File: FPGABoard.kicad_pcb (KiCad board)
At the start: 2 copper layers, 100 x 80 mm, 76 parts, among them P1 JTAG_FPGA, P3 USB_B, P4 CONN_02X07, P5 JTAG, P6 CONN_02X07, P7 CONN_02X07, P8 CONN_02X07, Q1 Q_NMOS_DSG, SW1 SW_PUSH, SW2 SW_PUSH, U1 XC3S50A/VQ100, U2 LM317_SOT223, U3 LM317_SOT223, U4 LM317_SOT223, U5 ATMEGA32U4RC-A, U6 M25P20, Y1 12MHz

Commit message: Layouting
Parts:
- removed REF**: EuroBoard_halb_Type-I_100mmX80mm_holes, EuroBoard_Outline:EuroBoard_halb_Type-I_100mmX80mm_holes
- added P2: CONN_02X03, w_pin_strip:pin_strip_3x2, F.Cu at (183.5, 71.8)
- R15, R17, R18: moved to B.Cu
- moved R8 43.8 mm to (109.2, 83.8)
- moved C17 41.3 mm to (120.0, 82.5)
- moved R4 41.3 mm to (113.0, 82.5)
- moved U2 40.6 mm to (114.3, 89.5)
- moved C16 40.6 mm to (119.4, 87.0)
- moved R2 40.6 mm to (139.7, 89.5)
- moved C20 36.7 mm to (147.3, 92.1)
- moved R10 36.7 mm to (157.5, 92.1)
- moved R6 36.3 mm to (156.2, 96.5)
- moved U4 36.3 mm to (152.4, 90.2)
- moved C21 36.3 mm to (149.2, 96.5)
- moved C19 24.2 mm to (116.8, 106.7)
- moved R5 23.8 mm to (110.5, 106.7)
- moved U3 23.3 mm to (114.3, 113.7)
- moved C18 23.3 mm to (119.4, 111.1)
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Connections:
- U1 pad 82: (no net) -> /Connections/BTN2
- U1 pad 97: (no net) -> /Connections/BTN1
- U5 pad 18: (no net) -> /Connections/C_IO2
- U5 pad 19: (no net) -> /Connections/C_IO3
- U5 pad 25: (no net) -> /Connections/C_IO4
- U5 pad 31: (no net) -> /Connections/C_IO1
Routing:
- net VCC: track 48.4 -> 389.7 mm, vias 0 -> 11
- net VCC_AUX: track 43.3 -> 128.4 mm, vias 1 -> 4
- net Net-(P5-Pad1): track 65.1 -> 0.64 mm, vias 1 -> 0
- net /Microcontroller/SCK: track 91.5 -> 28.2 mm, vias 2 -> 0
- net /Spartan3A/Clock_In: track 63.3 -> 0.00 mm, vias 4 -> 0
- net Net-(P5-Pad3): track 62.2 -> 0.00 mm, vias 1 -> 0
- net Net-(P5-Pad5): track 60.2 -> 0.00 mm, vias 1 -> 0
- net /Microcontroller/MISO: track 67.8 -> 8.01 mm, vias 4 -> 0
- net Net-(P5-Pad9): track 59.7 -> 0.00 mm
- net VCC_INT: track 7.17 -> 65.7 mm, vias 0 -> 4
- net /Microcontroller/CS_FPGA: track 58.2 -> 0.07 mm, vias 2 -> 0
- net /Connections/BTN1: track 0.00 -> 56.6 mm, vias 0 -> 2
- net /Microcontroller/RESET: track 55.3 -> 0.00 mm, vias 2 -> 0
- net /Microcontroller/DONE: track 73.9 -> 22.1 mm, vias 2 -> 0
- net /Microcontroller/PROG_B: track 49.4 -> 3.36 mm, vias 2 -> 0
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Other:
- board outline removed
- net class Supply added: clearance 0.1, trace_width 0.5, via_dia 0.6, via_drill 0.4

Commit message: Layout
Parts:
- added C30: 1µF, Capacitors_SMD:C_0805_HandSoldering, B.Cu at (131.1, 102.4)
- added C31: 1µF, Capacitors_SMD:C_0805_HandSoldering, B.Cu at (173.7, 66.5)
- added C32: 1µF, Capacitors_SMD:C_0805_HandSoldering, B.Cu at (145.5, 93.2)
- added C33: 1µF, Capacitors_SMD:C_0805_HandSoldering, B.Cu at (145.3, 96.5)
- added REF**: EuroBoard_halb_Type-I_100mmX80mm_holes, EuroBoard_Outline:EuroBoard_halb_Type-I_100mmX80mm_holes, F.Cu at (88.4, 140.5)
- added U7: XO53, Oscillator__Crystal_SMD:Oscillator_XO53, F.Cu at (156.5, 111.0)
- C1, C2, C7: moved to F.Cu
- C17, C19, C21: footprint Capacitors_Tantalum_SMD:TantalC_SizeA_EIA-3216_HandSoldering -> Capacitors_SMD:C_0805_HandSoldering
- C22: moved to B.Cu
- C23, C24, C25, C26, C27, C29: footprint Capacitors_SMD:C_0603_HandSoldering -> Capacitors_SMD:C_0805_HandSoldering
- P3: footprint Connect:USB_B -> w_conn_pc:conn_usb_B_mini_smd
- Y1: footprint Crystals:Crystal_HC49-SD_SMD -> w_crystal:hc-49_smd
- moved C1 71.3 mm to (156.7, 107.4), turned to 180 degrees
- moved R10 53.6 mm to (109.5, 115.8)
- moved U4 50.4 mm to (114.3, 123.2), turned to 0 degrees
- moved R6 47.6 mm to (113.3, 117.1), turned to 180 degrees
- moved C21 40.3 mm to (113.3, 114.8)
- moved C20 38.9 mm to (119.1, 118.9)
- moved R18 15.1 mm to (100.3, 108.0)
- moved R17 15.0 mm to (100.3, 105.2)
- moved R15 14.9 mm to (100.3, 102.4)
- moved R9 12.5 mm to (109.7, 99.3), turned to 90 degrees
- moved P3 9.90 mm to (139.5, 66.0), turned to 180 degrees
- moved C19 9.11 mm to (113.3, 98.3), turned to 180 degrees
- moved U3 7.11 mm to (114.3, 106.6)
- moved C17 6.85 mm to (113.3, 81.3), turned to 180 degrees
- moved R5 6.71 mm to (113.3, 100.6)
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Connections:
- D5 pad 1: GND -> Net-(D5-Pad1)
- D5 pad 2: Net-(D5-Pad2) -> /Connections/LED2
- D6 pad 1: GND -> Net-(D6-Pad1)
- D6 pad 2: Net-(D6-Pad2) -> /Connections/LED1
- D7 pad 1: GND -> Net-(D7-Pad1)
- D7 pad 2: Net-(D7-Pad2) -> /Connections/LED3
- P2 pad 1: (no net) -> VCC
- P2 pad 2: (no net) -> GND
- R1 pad 1: /Microcontroller/PROG_B -> Net-(R1-Pad1)
- R15 pad 1: Net-(D5-Pad2) -> GND
- R15 pad 2: /Connections/LED2 -> Net-(D6-Pad1)
- R17 pad 1: Net-(D6-Pad2) -> GND
- R17 pad 2: /Connections/LED1 -> Net-(D5-Pad1)
- R18 pad 1: Net-(D7-Pad2) -> GND
- R18 pad 2: /Connections/LED3 -> Net-(D7-Pad1)
- U1 pad 100: /Microcontroller/PROG_B -> Net-(R1-Pad1)
- U1 pad 90: /Spartan3A/Clock_In -> Net-(U1-Pad90)
- U5 pad 28: /Microcontroller/PROG_B -> (no net)
- U5 pad 32: /Spartan3A/Clock_In -> (no net)
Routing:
- net /Microcontroller/DONE: track 22.1 -> 107.0 mm, vias 0 -> 3
- net /Microcontroller/CS_FPGA: track 0.07 -> 63.8 mm, vias 0 -> 4
- net /Microcontroller/INIT_B: track 6.04 -> 69.3 mm, vias 0 -> 4
- net /Microcontroller/CS_FLASH: track 0.47 -> 59.4 mm, vias 0 -> 3
- net /Microcontroller/SCK: track 28.2 -> 85.7 mm, vias 0 -> 4
- net /Microcontroller/MISO: track 8.01 -> 59.3 mm, vias 0 -> 4
- net /Microcontroller/MOSI: track 26.5 -> 75.5 mm, vias 0 -> 4
- net /Microcontroller/CS_C: track 0.00 -> 37.1 mm
- net VCC: track 389.7 -> 425.3 mm, vias 11 -> 12
- net /Microcontroller/V_USB: track 70.5 -> 35.2 mm, vias 1 -> 5
- net /Connections/LED1: track 0.00 -> 28.9 mm, vias 0 -> 2
- net /Connections/LED2: track 0.00 -> 24.2 mm, vias 0 -> 2
- net /Connections/C_IO3: track 0.00 -> 23.3 mm, vias 0 -> 1
- net VCC_AUX: track 128.4 -> 105.5 mm
- net /Connections/LED3: track 0.00 -> 20.0 mm, vias 0 -> 2
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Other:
- board outline added: 100 x 80 mm

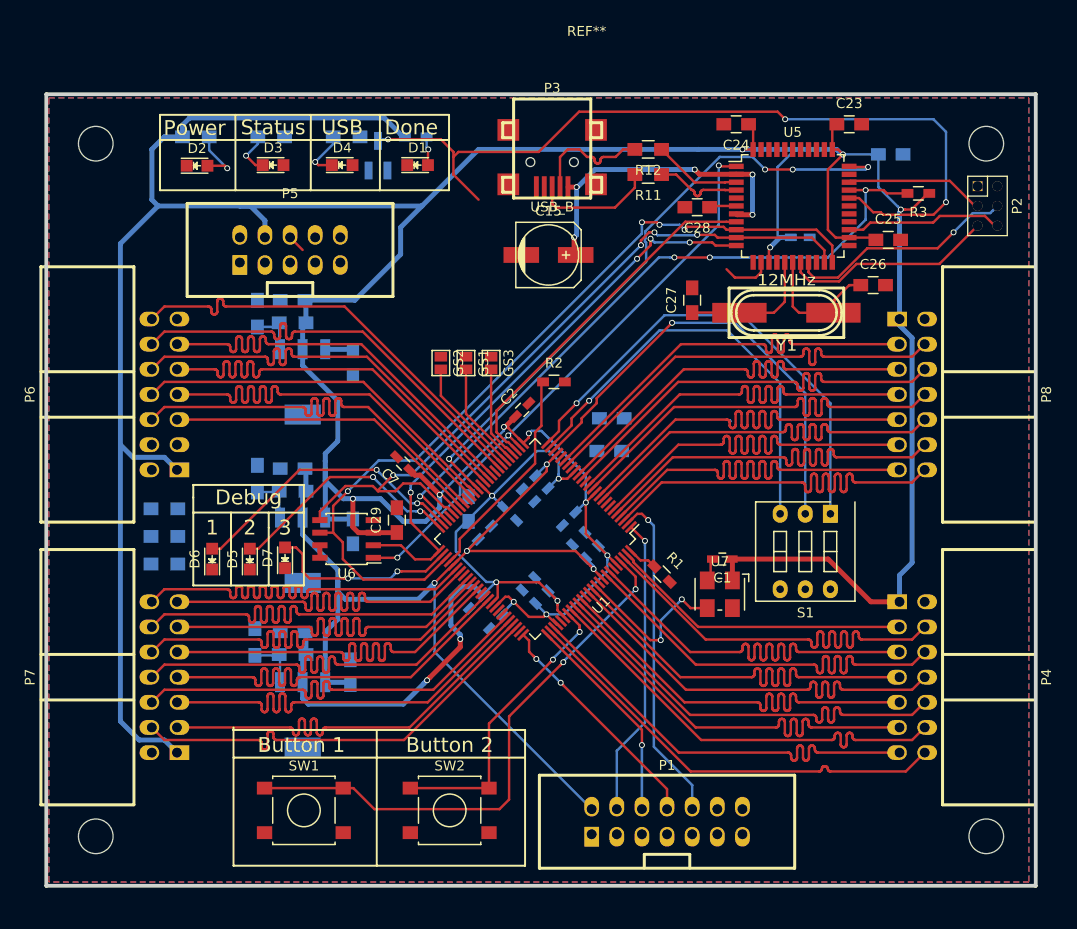
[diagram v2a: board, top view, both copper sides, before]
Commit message: Additional Caps at VCC, Layout
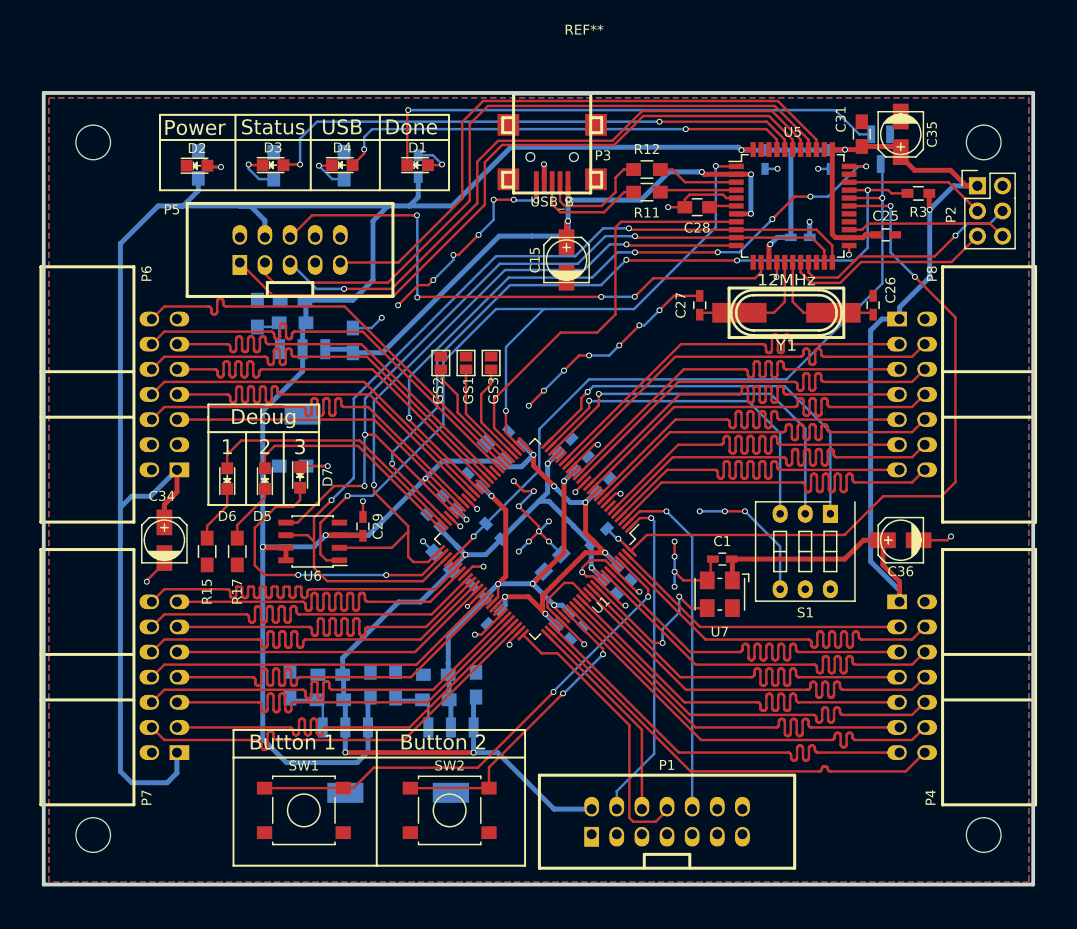
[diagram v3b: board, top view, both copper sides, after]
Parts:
- added C34: 10µF, Capacitors_SMD:c_elec_4x5.8, F.Cu at (100.3, 105.5)
- added C35: 10µF, Capacitors_SMD:c_elec_4x5.8, F.Cu at (174.8, 64.5)
- added C36: 10µF, Capacitors_SMD:c_elec_4x5.8, F.Cu at (174.8, 105.5)
- C15: footprint Capacitors_SMD:c_elec_6.3x4.5 -> Capacitors_SMD:c_elec_4x5.8
- C2, C7, R1, R2: moved to B.Cu
- C23, C24: footprint Capacitors_SMD:C_0805_HandSoldering -> Capacitors_SMD:C_0603_HandSoldering; moved to B.Cu
- C25, C26, C27, C29: footprint Capacitors_SMD:C_0805_HandSoldering -> Capacitors_SMD:C_0603_HandSoldering
- C31, R15, R17: moved to F.Cu
- P2: footprint w_pin_strip:pin_strip_3x2 -> Pin_Headers:Pin_Header_Straight_2x03
- moved Q1 50.8 mm to (172.7, 66.0), turned to 0 degrees
- moved C32 22.3 mm to (128.5, 107.7), turned to 135 degrees
- moved U3 21.6 mm to (118.6, 127.8)
- moved R5 21.4 mm to (117.1, 121.7)
- moved C19 21.2 mm to (117.1, 119.1)
- moved R9 21.1 mm to (113.0, 120.1)
- moved R18 16.3 mm to (113.3, 98.0)
- moved R2 16.3 mm to (133.6, 104.6), turned to 315 degrees
- moved U4 15.7 mm to (129.3, 127.8)
- moved C18 15.6 mm to (121.2, 120.1), turned to 90 degrees
- moved R6 15.2 mm to (127.8, 121.7)
- moved C21 15.1 mm to (127.8, 119.1)
- moved R10 14.9 mm to (123.7, 120.1)
- moved C20 12.8 mm to (131.8, 120.1)
- moved C33 12.7 mm to (139.6, 107.8), turned to 45 degrees
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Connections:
- R1 pad 1: Net-(R1-Pad1) -> /Microcontroller/PROG_B
- U1 pad 100: Net-(R1-Pad1) -> /Microcontroller/PROG_B
- U5 pad 28: (no net) -> /Microcontroller/PROG_B
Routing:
- net GND: track 3.35 -> 158.8 mm, vias 0 -> 54
- net /Microcontroller/PROG_B: track 0.00 -> 73.8 mm, vias 0 -> 3
- net Net-(P5-Pad3): track 0.00 -> 70.8 mm
- net Net-(P5-Pad1): track 0.64 -> 69.9 mm
- net Net-(P5-Pad5): track 0.00 -> 64.8 mm, vias 0 -> 1
- net Net-(P5-Pad9): track 0.00 -> 62.0 mm
- net Net-(D3-Pad2): track 0.45 -> 56.2 mm, vias 0 -> 2
- net Net-(D1-Pad1): track 0.00 -> 53.4 mm, vias 0 -> 1
- net /Microcontroller/RESET: track 6.86 -> 58.9 mm, vias 0 -> 4
- net Net-(D4-Pad2): track 0.04 -> 46.8 mm, vias 0 -> 2
- net /Microcontroller/DONE: track 107.0 -> 73.4 mm, vias 3 -> 2
- net VCC: track 425.3 -> 458.4 mm, vias 12 -> 14
- net /Microcontroller/CS_FLASH: track 59.4 -> 86.2 mm
- net /Microcontroller/V_USB: track 35.2 -> 61.8 mm
- net VCC_INT: track 79.5 -> 58.8 mm, vias 6 -> 5
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
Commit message: Work in Progress
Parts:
- added G***: LOGO, Loewe:Loewe_Klein, F.Cu at (170.6, 130.2)
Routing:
- net GND: track 158.8 -> 263.8 mm, vias 54 -> 71
- net /Connections/GPIO31: track 0.00 -> 45.0 mm, vias 0 -> 1
- net /Connections/GPIO33: track 45.0 -> 37.3 mm
- net /Microcontroller/DC-: track 12.0 -> 13.4 mm
- net /Microcontroller/PROG_B: track 73.8 -> 75.3 mm
- net /Microcontroller/DC+: track 11.6 -> 13.0 mm
- net /Microcontroller/CS_FLASH: track 86.2 -> 87.3 mm
- net /Microcontroller/D+: track 7.77 -> 8.61 mm
- net /Microcontroller/V_USB: track 61.8 -> 62.5 mm
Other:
- board text added: "0"
- board text added: "AVR JTAG"
- board text added: "Controller"
- board text added: "EEPROM"
- board text added: "FPGA JTAG"
- board text added: "GPIO 0"
- board text added: "GPIO 1"
- board text added: "GPIO 2"
- board text added: "GPIO 3"
- board text added: "JTAG"
- board text added: "LV 0"
- board text added: "LV 1"
- board text added: "LV 2"
- board text added: "Progr. Mode"
- board text added: "Spartan 3A Eval-Board"
- board text added: "v1.0 D. Walter"

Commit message: Small update
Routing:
- net /Microcontroller/MISO: track 71.9 -> 72.4 mm

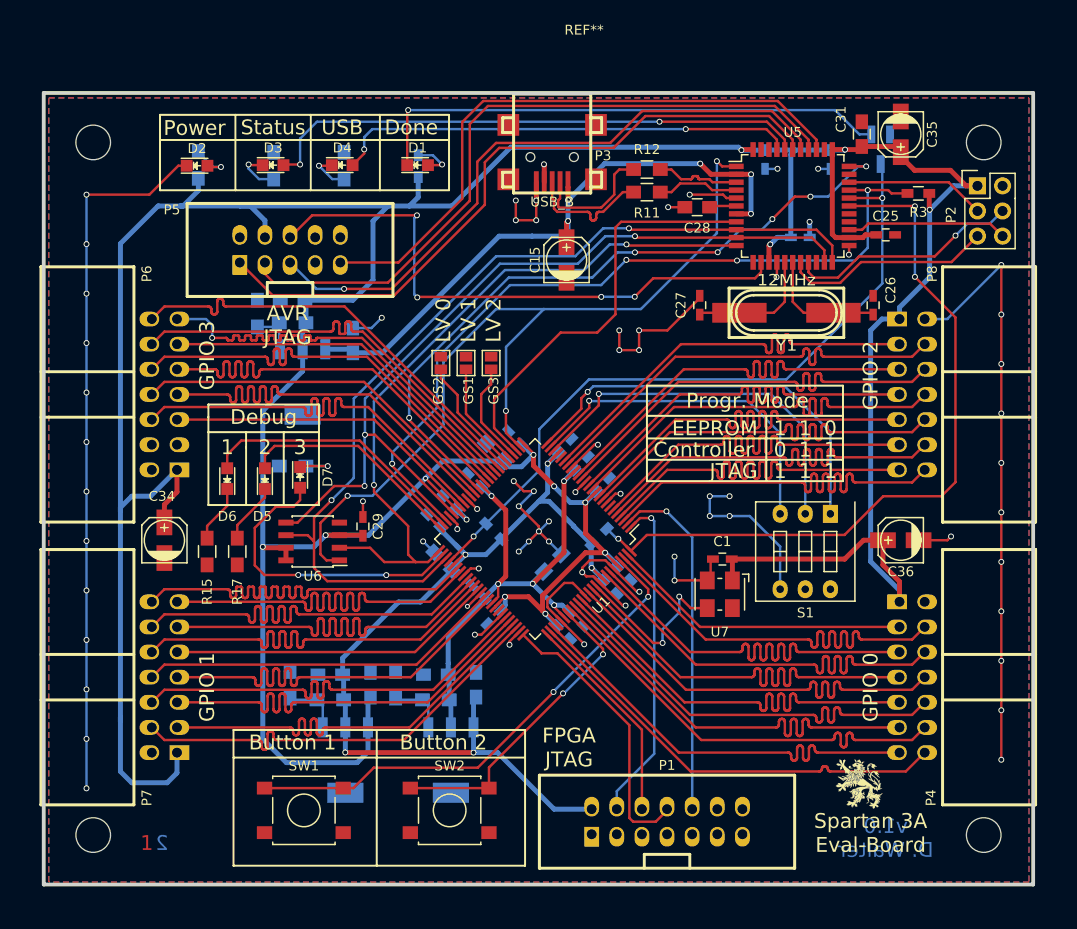
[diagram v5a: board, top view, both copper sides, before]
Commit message: All Resistors 0805, New Buttons
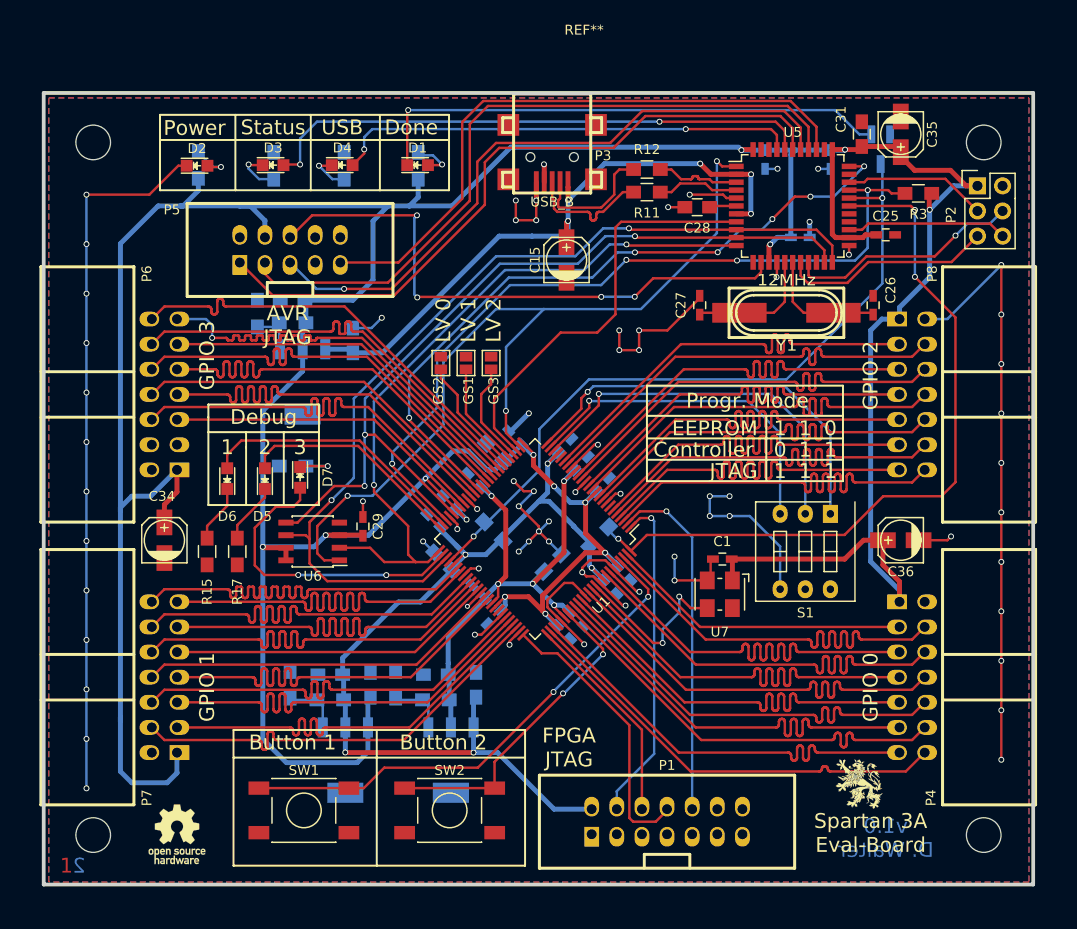
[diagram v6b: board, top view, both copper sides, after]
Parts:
- added REF***: OSHW-Logo_5.7x6mm_SilkScreen, Symbols:OSHW-Logo_5.7x6mm_SilkScreen, F.Cu at (101.6, 135.3)
- R1, R2, R3: footprint Resistors_SMD:R_0603_HandSoldering -> Resistors_SMD:R_0805_HandSoldering
- R13, R14, R15, R17, R18, R7: value 180R -> 100R
- R16: value 180R -> 100R; footprint Resistors_SMD:R_0603_HandSoldering -> Resistors_SMD:R_0805_HandSoldering
- SW1, SW2: footprint Buttons_Switches_SMD:SW_SPST_B3S-1000 -> SMD_Switch_LSX1301:SW_LSx_1301
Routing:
- net GND: track 263.8 -> 266.6 mm, vias 71 -> 72
- net Net-(P5-Pad9): track 62.0 -> 62.8 mm
- net Net-(P5-Pad3): track 70.8 -> 71.6 mm
- net Net-(P5-Pad5): track 64.8 -> 65.5 mm
- net Net-(P5-Pad1): track 69.9 -> 70.6 mm
- net /Connections/BTN1: track 51.6 -> 52.1 mm
- net Net-(D3-Pad2): track 56.2 -> 56.7 mm
